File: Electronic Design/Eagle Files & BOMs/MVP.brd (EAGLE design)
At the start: 88.6 x 68 mm, 35 parts, among them IC1 ACS712ELC-5A, IC2 ATMEGA328-PU, Q1 IRF9540, Q2 IRF9540, X1 16MHz

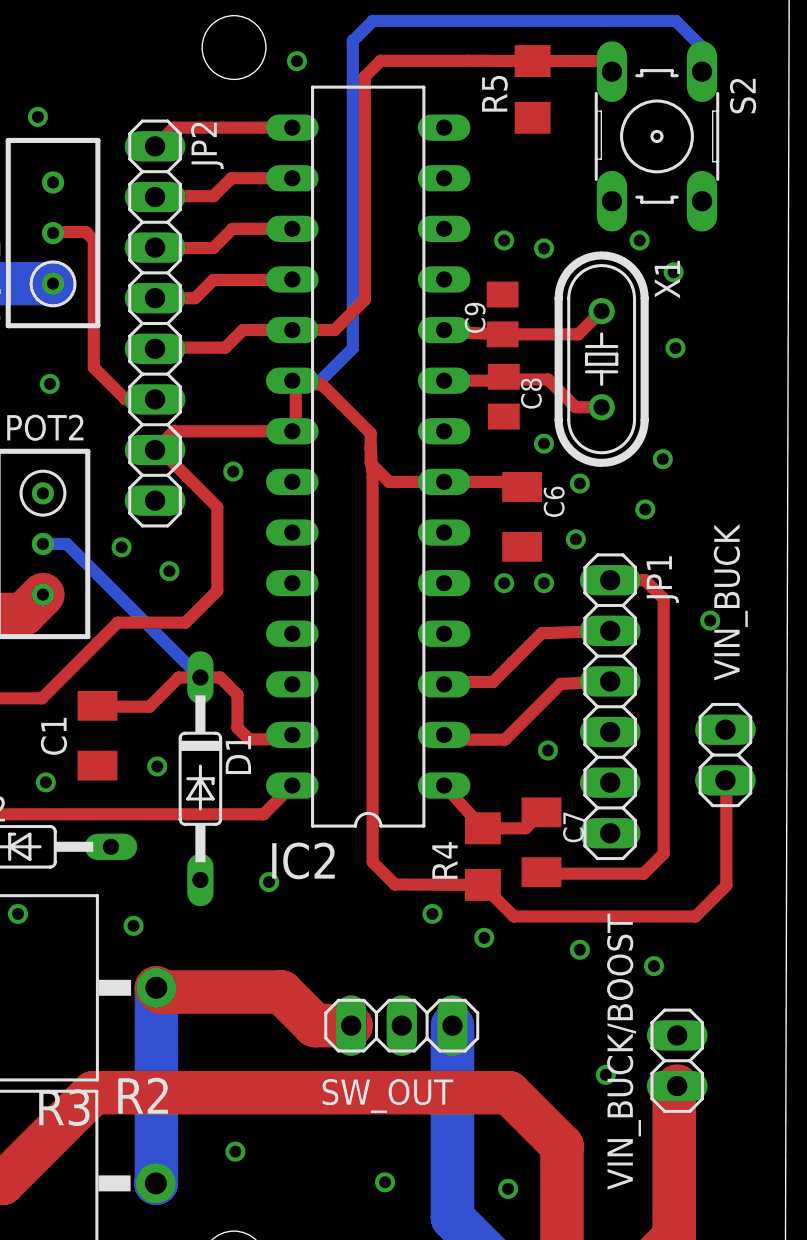
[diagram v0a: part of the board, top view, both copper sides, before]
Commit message: updating folder structure and improving naming in MVP board
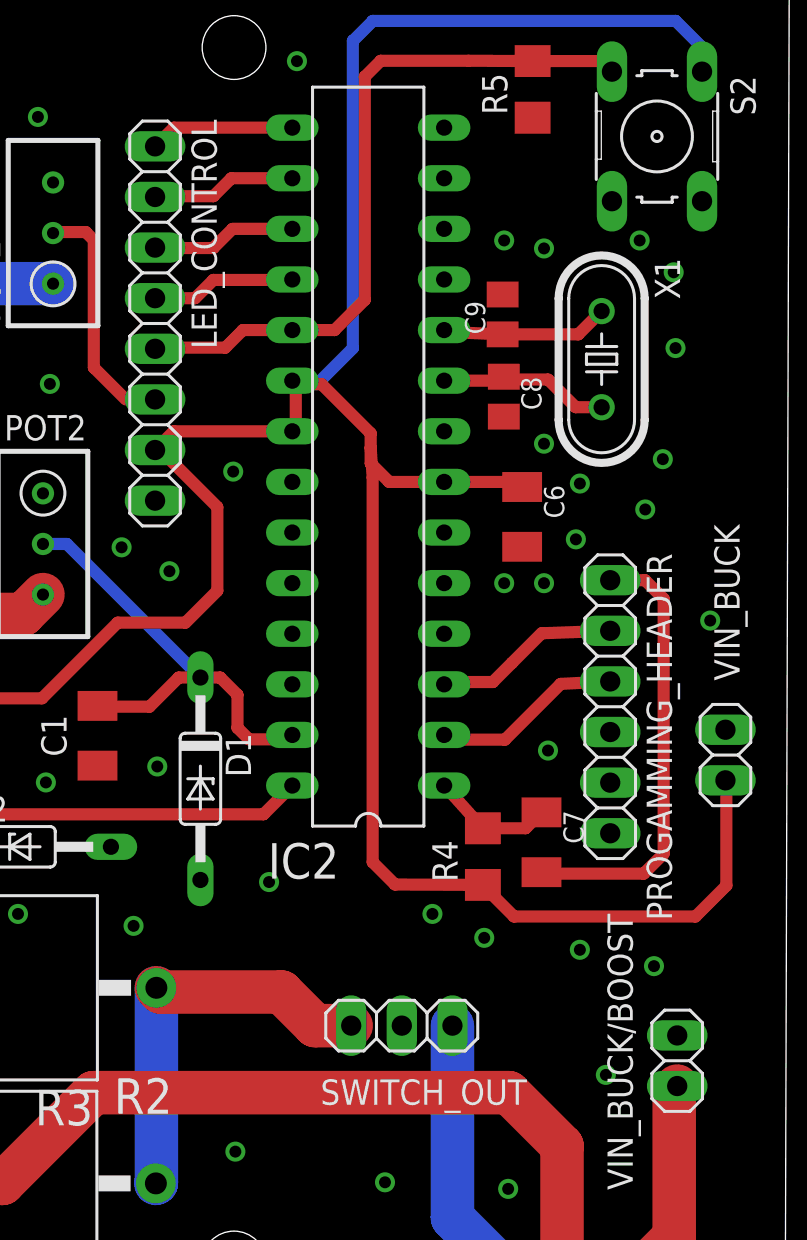
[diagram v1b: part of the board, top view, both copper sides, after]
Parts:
- renumbered JP1 to PROGAMMING_HEADER, JP2 to LED_CONTROL, SW_OUT to SWITCH_OUT
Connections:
- net OVERV renamed OVER_VOLTAGE
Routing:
- net OVER_VOLTAGE: track 12.4 -> 10.9 mm
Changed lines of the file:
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@@
 <element name="C9" library="resistor" package="C0805K" value="22n" x="74.320996875" y="51.667596875" rot="R90"/>
 <element name="C8" library="resistor" package="C0805K" value="22n" x="74.379803125" y="47.5407875" rot="R270"/>
-<element name="JP2" library="pinhead" package="1X08" value="" x="56.8750375" y="51.21298125" rot="R270"/>
+<element name="LED_CONTROL" library="pinhead" package="1X08" value="" x="56.8750375" y="51.21298125" rot="R270"/>
 <element name="VOUT-" library="pinhead" package="1X02" value="" x="3.49730625" y="34.2068625" smashed="yes" rot="R90">
 <attribute name="NAME" x="6.04288125" y="36.4397375" size="1.27" layer="25" ratio="10" rot="R270"/>
@@
 </element>
 <element name="VIN_BUCK" library="pinhead" package="1X02" value="" x="85.50119375" y="29.554190625" rot="R90"/>
-<element name="JP1" library="pinhead" package="1X06" value="" x="79.718590625" y="31.978721875" rot="R270"/>
+<element name="PROGAMMING_HEADER" library="pinhead" package="1X06" value="" x="79.718590625" y="31.978721875" rot="R270"/>
 <element name="C6" library="resistor" package="C1206K" value="10u" x="75.29648125" y="41.50599375" rot="R270"/>
 <element name="VIN_BUCK/BOOST" library="pinhead" package="1X02" value="" x="83.0813125" y="14.21156875" smashed="yes" rot="R90">
@@
 <element name="D1" library="diode" package="DO35Z10" value="5.1V" x="59.1502" y="28.3643125" rot="R270"/>
 <element name="C4" library="resistor" package="C1206K" value="0.1u" x="40.8393625" y="25.892384375" rot="R90"/>
-<element name="SW_OUT" library="pinhead" package="1X03" value="" x="69.258925" y="15.973903125" smashed="yes" rot="R180">
+<element name="SWITCH_OUT" library="pinhead" package="1X03" value="" x="69.258925" y="15.973903125" smashed="yes" rot="R180">
 <attribute name="NAME" x="65.172725" y="12.002703125" size="1.27" layer="25" ratio="10"/>
 <attribute name="VALUE" x="73.068925" y="19.148903125" size="1.27" layer="27" rot="R180"/>
@@
 <contactref element="C1" pad="2"/>
 <contactref element="POT2" pad="1"/>
-<contactref element="JP2" pad="8"/>
+<contactref element="LED_CONTROL" pad="8"/>
 <contactref element="D1" pad="A"/>
 <polygon width="0.6096" layer="1" isolate="0.3">
@@
 <via x="70.79569375" y="21.5802" extent="1-16" drill="0.6" shape="square"/>
 <contactref element="R5" pad="1"/>
-<contactref element="JP1" pad="6"/>
+<contactref element="PROGAMMING_HEADER" pad="6"/>
 <via x="32.99569375" y="33.1802" extent="1-16" drill="0.6" shape="square"/>
 <via x="37.39569375" y="28.5802" extent="1-16" drill="0.6" shape="square"/>
@@
 <contactref element="VOUT-" pad="2"/>
 <contactref element="VIN_BUCK" pad="2"/>
-<contactref element="SW_OUT" pad="2"/>
+<contactref element="SWITCH_OUT" pad="2"/>
 <contactref element="VIN_BUCK/BOOST" pad="2"/>
 </signal>
@@
 <wire x1="71.3825375" y1="43.262928125" x2="74.89648125" y2="43.262928125" width="0.6096" layer="1"/>
 <wire x1="74.89648125" y1="43.262928125" x2="75.29648125" y2="43.00599375" width="0.6096" layer="1"/>
-<contactref element="JP2" pad="7"/>
+<contactref element="LED_CONTROL" pad="7"/>
 <contactref element="IC1" pad="8"/>
 <contactref element="C3" pad="1"/>
@@
 <contactref element="S2" pad="3"/>
 <contactref element="R5" pad="2"/>
-<contactref element="JP2" pad="5"/>
+<contactref element="LED_CONTROL" pad="5"/>
 <wire x1="63.7625375" y1="50.882928125" x2="61.282928125" y2="50.882928125" width="0.6096" layer="1"/>
 <wire x1="61.282928125" y1="50.882928125" x2="60.4" y2="50" width="0.6096" layer="1"/>
@@
 </signal>
 <signal name="N$4">
-<contactref element="JP1" pad="2"/>
+<contactref element="PROGAMMING_HEADER" pad="2"/>
 <contactref element="IC2" pad="3"/>
 <wire x1="79.718590625" y1="35.788721875" x2="76.276234375" y2="35.665775" width="0.6096" layer="1"/>
@@
 </signal>
 <signal name="N$5">
-<contactref element="JP1" pad="3"/>
+<contactref element="PROGAMMING_HEADER" pad="3"/>
 <contactref element="IC2" pad="2"/>
 <wire x1="79.718590625" y1="33.248721875" x2="77.233571875" y2="33.125775" width="0.6096" layer="1"/>
@@
 </signal>
 <signal name="N$14">
-<contactref element="JP1" pad="1"/>
+<contactref element="PROGAMMING_HEADER" pad="1"/>
 <contactref element="C7" pad="2"/>
 <wire x1="79.718590625" y1="38.328721875" x2="81.471278125" y2="38.328721875" width="0.6096" layer="1"/>
@@
 <contactref element="R2" pad="1"/>
 <contactref element="R3" pad="1"/>
-<contactref element="SW_OUT" pad="3"/>
+<contactref element="SWITCH_OUT" pad="3"/>
 <wire x1="66.718925" y1="15.973903125" x2="64.906096875" y2="15.973903125" width="2.1844" layer="1"/>
 <wire x1="64.906096875" y1="15.973903125" x2="63.22" y2="17.66" width="2.1844" layer="1"/>
@@
 </signal>
 <signal name="N$25">
-<contactref element="SW_OUT" pad="1"/>
+<contactref element="SWITCH_OUT" pad="1"/>
 <contactref element="USB_OUT" pad="2"/>
 <wire x1="71.798925" y1="15.973903125" x2="71.798925" y2="6.330475" width="2.1844" layer="16"/>
@@
 <signal name="N$6">
 <contactref element="IC2" pad="15"/>
-<contactref element="JP2" pad="1"/>
+<contactref element="LED_CONTROL" pad="1"/>
 <wire x1="63.7625375" y1="61.042928125" x2="57.814984375" y2="61.042928125" width="0.6096" layer="1"/>
 <wire x1="57.814984375" y1="61.042928125" x2="56.8750375" y2="60.10298125" width="0.6096" layer="1"/>
 </signal>
 <signal name="N$9">
-<contactref element="JP2" pad="2"/>
+<contactref element="LED_CONTROL" pad="2"/>
 <contactref element="IC2" pad="16"/>
 <wire x1="63.7625375" y1="58.502928125" x2="60.702928125" y2="58.502928125" width="0.6096" layer="1"/>
@@
 <signal name="N$11">
 <contactref element="IC2" pad="17"/>
-<contactref element="JP2" pad="3"/>
+<contactref element="LED_CONTROL" pad="3"/>
 <wire x1="63.7625375" y1="55.962928125" x2="60.762928125" y2="55.962928125" width="0.6096" layer="1"/>
 <wire x1="60.762928125" y1="55.962928125" x2="59.8" y2="55" width="0.6096" layer="1"/>
@@
 <signal name="N$12">
 <contactref element="IC2" pad="18"/>
-<contactref element="JP2" pad="4"/>
+<contactref element="LED_CONTROL" pad="4"/>
 <wire x1="56.8750375" y1="52.48298125" x2="58.88298125" y2="52.48298125" width="0.6096" layer="1"/>
 <wire x1="58.88298125" y1="52.48298125" x2="59.8" y2="53.4" width="0.6096" layer="1"/>
 <wire x1="59.8" y1="53.4" x2="63.739609375" y2="53.4" width="0.6096" layer="1"/>
 <wire x1="63.739609375" y1="53.4" x2="63.7625375" y2="53.422928125" width="0.6096" layer="1"/>
-</signal>
-<signal name="OVERV">
-<contactref element="POT1" pad="2"/>
-<contactref element="JP2" pad="6"/>
-<wire x1="56.8750375" y1="47.40298125" x2="55.39701875" y2="47.40298125" width="0.6096" layer="1"/>
-<wire x1="55.39701875" y1="47.40298125" x2="53.8" y2="49" width="0.6096" layer="1"/>
-<wire x1="53.8" y1="49" x2="53.8" y2="55.4" width="0.6096" layer="1"/>
-<wire x1="53.8" y1="55.4" x2="53.4" y2="55.8" width="0.6096" layer="1"/>
-<wire x1="53.4" y1="55.8" x2="51.80363125" y2="55.8" width="0.6096" layer="1"/>
-<wire x1="51.80363125" y1="55.8" x2="51.755203125" y2="55.751571875" width="0.6096" layer="1"/>
 </signal>
 <signal name="N$2">
@@
 <wire x1="18.6" y1="30.920446875" x2="18.775396875" y2="30.74505" width="2.1844" layer="1"/>
 </signal>
+<signal name="OVER_VOLTAGE">
+<contactref element="LED_CONTROL" pad="6"/>
+<contactref element="POT1" pad="2"/>
+<wire x1="55.39701875" y1="47.40298125" x2="53.8" y2="49" width="0.6096" layer="1"/>
+<wire x1="53.8" y1="49" x2="53.8" y2="55.4" width="0.6096" layer="1"/>
+<wire x1="53.8" y1="55.4" x2="53.4" y2="55.8" width="0.6096" layer="1"/>
+<wire x1="53.4" y1="55.8" x2="51.80363125" y2="55.8" width="0.6096" layer="1"/>
+<wire x1="51.80363125" y1="55.8" x2="51.755203125" y2="55.751571875" width="0.6096" layer="1"/>
+<wire x1="55.39701875" y1="47.40298125" x2="56.8750375" y2="47.40298125" width="0" layer="19" extent="1-1"/>
+</signal>
 </signals>

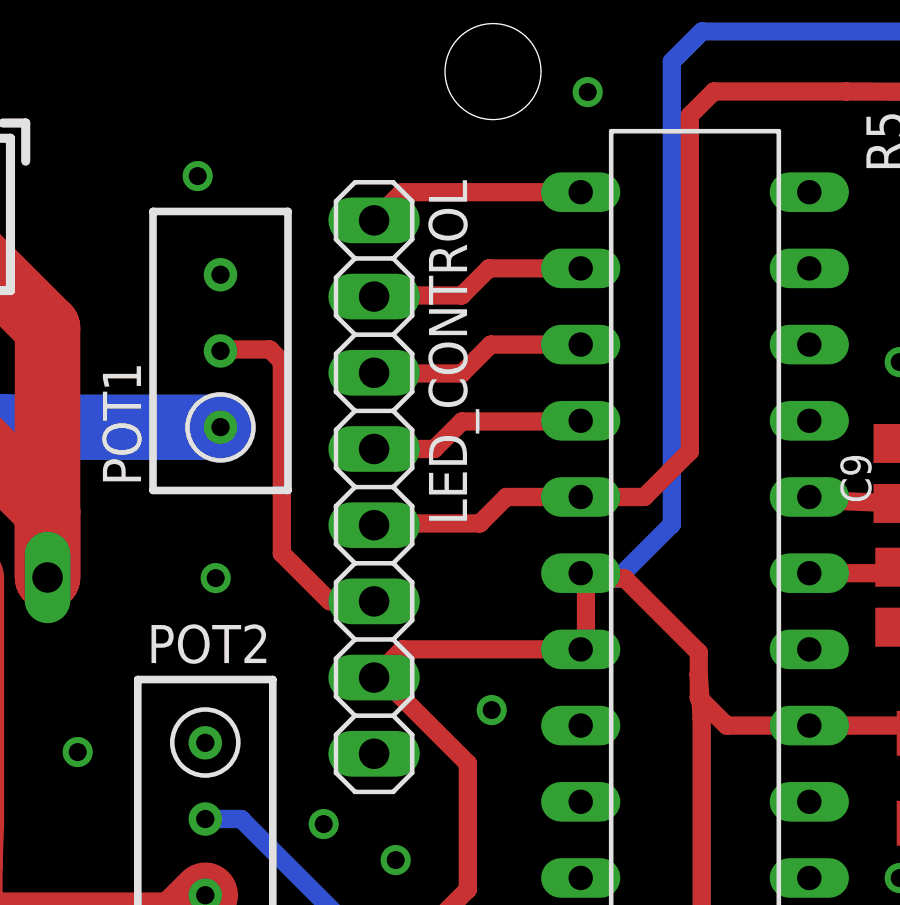
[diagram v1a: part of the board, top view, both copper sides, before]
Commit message: changed that name of header to LED_CONTROL_IN / OUT
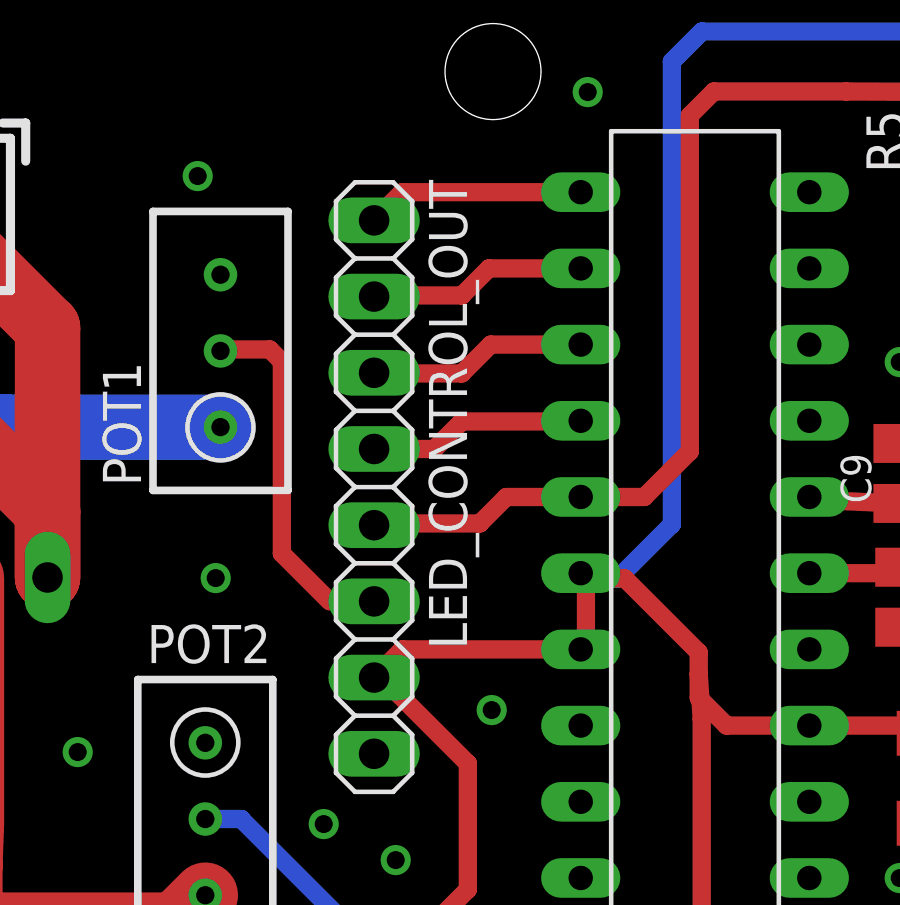
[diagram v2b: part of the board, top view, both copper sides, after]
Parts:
- renumbered LED_CONTROL to LED_CONTROL_OUT
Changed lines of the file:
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@@
 <element name="C9" library="resistor" package="C0805K" value="22n" x="74.320996875" y="51.667596875" rot="R90"/>
 <element name="C8" library="resistor" package="C0805K" value="22n" x="74.379803125" y="47.5407875" rot="R270"/>
-<element name="LED_CONTROL" library="pinhead" package="1X08" value="" x="56.8750375" y="51.21298125" rot="R270"/>
+<element name="LED_CONTROL_OUT" library="pinhead" package="1X08" value="" x="56.8750375" y="51.21298125" rot="R270"/>
 <element name="VOUT-" library="pinhead" package="1X02" value="" x="3.49730625" y="34.2068625" smashed="yes" rot="R90">
 <attribute name="NAME" x="6.04288125" y="36.4397375" size="1.27" layer="25" ratio="10" rot="R270"/>
@@
 <contactref element="C1" pad="2"/>
 <contactref element="POT2" pad="1"/>
-<contactref element="LED_CONTROL" pad="8"/>
+<contactref element="LED_CONTROL_OUT" pad="8"/>
 <contactref element="D1" pad="A"/>
 <polygon width="0.6096" layer="1" isolate="0.3">
@@
 <wire x1="71.3825375" y1="43.262928125" x2="74.89648125" y2="43.262928125" width="0.6096" layer="1"/>
 <wire x1="74.89648125" y1="43.262928125" x2="75.29648125" y2="43.00599375" width="0.6096" layer="1"/>
-<contactref element="LED_CONTROL" pad="7"/>
+<contactref element="LED_CONTROL_OUT" pad="7"/>
 <contactref element="IC1" pad="8"/>
 <contactref element="C3" pad="1"/>
@@
 <contactref element="S2" pad="3"/>
 <contactref element="R5" pad="2"/>
-<contactref element="LED_CONTROL" pad="5"/>
+<contactref element="LED_CONTROL_OUT" pad="5"/>
 <wire x1="63.7625375" y1="50.882928125" x2="61.282928125" y2="50.882928125" width="0.6096" layer="1"/>
 <wire x1="61.282928125" y1="50.882928125" x2="60.4" y2="50" width="0.6096" layer="1"/>
@@
 <signal name="N$6">
 <contactref element="IC2" pad="15"/>
-<contactref element="LED_CONTROL" pad="1"/>
+<contactref element="LED_CONTROL_OUT" pad="1"/>
 <wire x1="63.7625375" y1="61.042928125" x2="57.814984375" y2="61.042928125" width="0.6096" layer="1"/>
 <wire x1="57.814984375" y1="61.042928125" x2="56.8750375" y2="60.10298125" width="0.6096" layer="1"/>
 </signal>
 <signal name="N$9">
-<contactref element="LED_CONTROL" pad="2"/>
+<contactref element="LED_CONTROL_OUT" pad="2"/>
 <contactref element="IC2" pad="16"/>
 <wire x1="63.7625375" y1="58.502928125" x2="60.702928125" y2="58.502928125" width="0.6096" layer="1"/>
@@
 <signal name="N$11">
 <contactref element="IC2" pad="17"/>
-<contactref element="LED_CONTROL" pad="3"/>
+<contactref element="LED_CONTROL_OUT" pad="3"/>
 <wire x1="63.7625375" y1="55.962928125" x2="60.762928125" y2="55.962928125" width="0.6096" layer="1"/>
 <wire x1="60.762928125" y1="55.962928125" x2="59.8" y2="55" width="0.6096" layer="1"/>
@@
 <signal name="N$12">
 <contactref element="IC2" pad="18"/>
-<contactref element="LED_CONTROL" pad="4"/>
+<contactref element="LED_CONTROL_OUT" pad="4"/>
 <wire x1="56.8750375" y1="52.48298125" x2="58.88298125" y2="52.48298125" width="0.6096" layer="1"/>
 <wire x1="58.88298125" y1="52.48298125" x2="59.8" y2="53.4" width="0.6096" layer="1"/>
@@
 </signal>
 <signal name="OVER_VOLTAGE">
-<contactref element="LED_CONTROL" pad="6"/>
+<contactref element="LED_CONTROL_OUT" pad="6"/>
 <contactref element="POT1" pad="2"/>
 <wire x1="55.39701875" y1="47.40298125" x2="53.8" y2="49" width="0.6096" layer="1"/>
